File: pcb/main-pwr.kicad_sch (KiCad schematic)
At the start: 0 parts

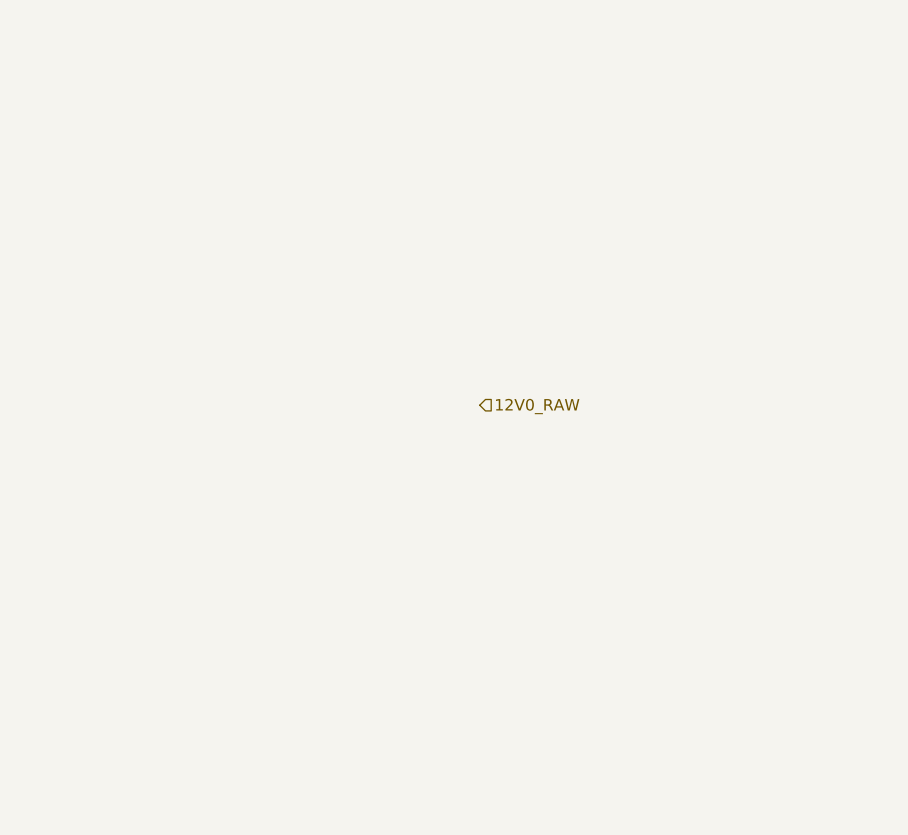
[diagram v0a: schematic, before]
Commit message: add eth phy
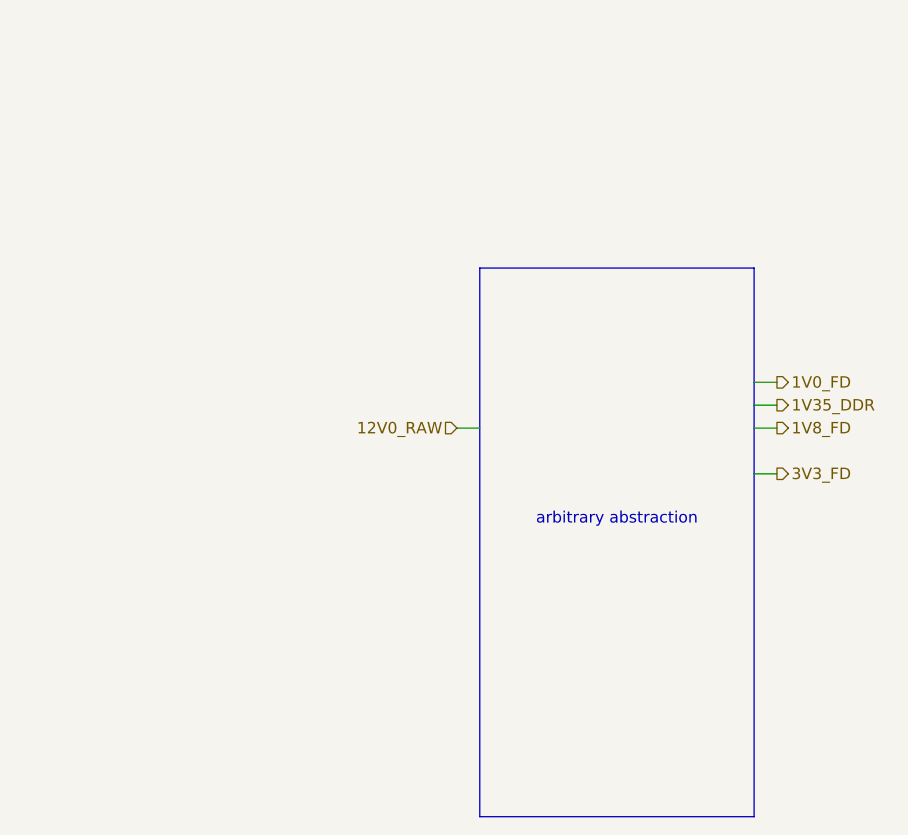
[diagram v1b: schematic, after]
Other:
- note added: "arbitrary abstraction"
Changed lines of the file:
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@@
 		(rev "2.0")
+	)
+	(rectangle
+		(start 132.08 71.12)
+		(end 162.56 132.08)
+		(stroke
+			(width 0)
+			(type default)
+		)
+		(fill
+			(type none)
+		)
+	)
+	(text "arbitrary abstraction"
+		(exclude_from_sim no)
+		(at 147.32 99.06 0)
+		(effects
+			(font
+				(size 1.27 1.27)
+			)
+		)
+	)
+	(wire
+		(pts
+			(xy 162.56 93.98) (xy 165.1 93.98)
+		)
+		(stroke
+			(width 0)
+			(type default)
+		)
+	)
+	(wire
+		(pts
+			(xy 129.54 88.9) (xy 132.08 88.9)
+		)
+		(stroke
+			(width 0)
+			(type default)
+		)
+	)
+	(wire
+		(pts
+			(xy 162.56 86.36) (xy 165.1 86.36)
+		)
+		(stroke
+			(width 0)
+			(type default)
+		)
+	)
+	(wire
+		(pts
+			(xy 162.56 83.82) (xy 165.1 83.82)
+		)
+		(stroke
+			(width 0)
+			(type default)
+		)
+	)
+	(wire
+		(pts
+			(xy 162.56 88.9) (xy 165.1 88.9)
+		)
+		(stroke
+			(width 0)
+			(type default)
+		)
+	)
+	(hierarchical_label "1V0_FD"
+		(shape output)
+		(at 165.1 83.82 0)
+		(effects
+			(font
+				(size 1.27 1.27)
+			)
+			(justify left)
+		)
 	)
 	(hierarchical_label "12V0_RAW"
 		(shape input)
-		(at 132.08 86.36 0)
+		(at 129.54 88.9 180)
 		(effects
 			(font
+				(size 1.27 1.27)
+			)
+			(justify right)
+		)
+	)
+	(hierarchical_label "3V3_FD"
+		(shape output)
+		(at 165.1 93.98 0)
+		(effects
+			(font
+				(size 1.27 1.27)
+			)
+			(justify left)
+		)
+	)
+	(hierarchical_label "1V8_FD"
+		(shape output)
+		(at 165.1 88.9 0)
+		(effects
+			(font
+				(size 1.27 1.27)
+			)
+			(justify left)
+		)
+	)
+	(hierarchical_label "1V35_DDR"
+		(shape output)
+		(at 165.1 86.36 0)
+		(effects
+			(font

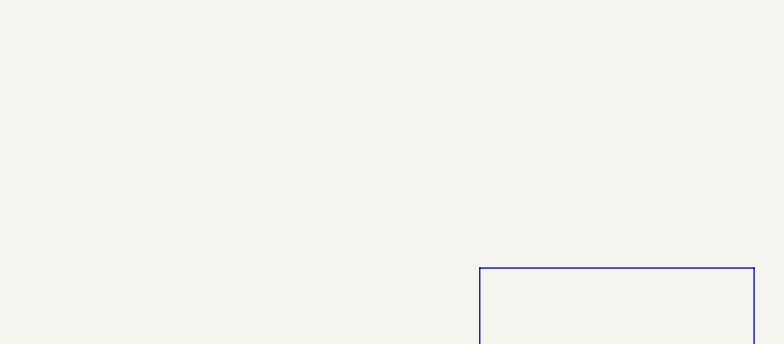
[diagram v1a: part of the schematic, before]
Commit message: phy and debug ffc conn
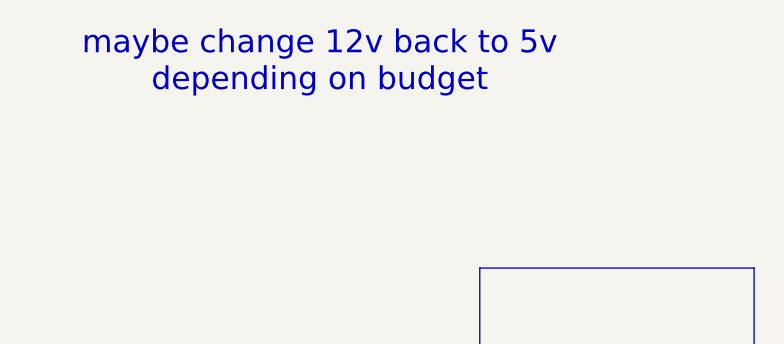
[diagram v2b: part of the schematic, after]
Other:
- note added: "maybe change 12v back to 5v depending on budget"
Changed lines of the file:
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@@
+		)
+	)
+	(text "maybe change 12v back to 5v\ndepending on budget"
+		(exclude_from_sim no)
+		(at 114.3 48.26 0)
+		(effects
+			(font
+				(size 2.54 2.54)
+			)
 		)
 	)
